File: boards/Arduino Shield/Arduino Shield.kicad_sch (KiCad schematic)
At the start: 22 parts, among them J1 Screw_Terminal_01x07, J10 Screw_Terminal_01x03, J11 Screw_Terminal_01x08, J2 Screw_Terminal_01x08, J3 Screw_Terminal_01x08, J4 Screw_Terminal_01x08, J5 Screw_Terminal_01x08, J6 Screw_Terminal_01x08, J7 Screw_Terminal_01x08, J8 Screw_Terminal_01x04, J9 Screw_Terminal_01x10, U1 A000062

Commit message: Fixed pcb and schematic.
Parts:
- removed J10: Screw_Terminal_01x03, TerminalBlock_4Ucon:TerminalBlock_4Ucon_1x03_P3.50mm_Horizontal, symbol Connector:Screw_Terminal_01x03
- removed J8: Screw_Terminal_01x04, TerminalBlock_4Ucon:TerminalBlock_4Ucon_1x04_P3.50mm_Horizontal, symbol Connector:Screw_Terminal_01x04
- added J8: Screw_Terminal_01x07, TerminalBlock_4Ucon:TerminalBlock_4Ucon_1x07_P3.50mm_Horizontal, symbol Connector:Screw_Terminal_01x07
- R4: value 230Ω -> 232Ω
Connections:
- net at U1.43 (D43): now also J8.4 (Pin_4)
- net at U1.45 (D45): now also J8.5 (Pin_5)
- net at U1.47 (D47): now also J8.6 (Pin_6)
- net at U1.GND5: now also J8.7 (Pin_7)
- net at U1.37 (D37): now also J8.1 (Pin_1)
- net at U1.39 (D39): now also J8.2 (Pin_2)
- net at U1.41 (D41): now also J8.3 (Pin_3)

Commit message: finished shield v1
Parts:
- renumbered D3 to D1, D4 to D2, D2 to D3, D5 to D4, D1 to D5
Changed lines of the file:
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@@
   (symbol (lib_id "Device:LED") (at 87.63 154.94 90) (unit 1)
     (in_bom yes) (on_board yes) (dnp no)
-    (property "Reference" "D5" (at 91.44 156.21 90)
+    (property "Reference" "D4" (at 91.44 156.21 90)
       (effects (font (size 1.27 1.27)))
     )
@@
       (project "Arduino Shield"
         (path "/d32bdb2e-fa3a-461a-9e34-c0053c91b5d5"
-          (reference "D5") (unit 1)
+          (reference "D4") (unit 1)
         )
       )
@@
   (symbol (lib_id "Device:LED") (at 162.56 153.67 90) (unit 1)
     (in_bom yes) (on_board yes) (dnp no) (fields_autoplaced)
-    (property "Reference" "D2" (at 166.37 153.9875 90)
+    (property "Reference" "D3" (at 166.37 153.9875 90)
       (effects (font (size 1.27 1.27)) (justify right))
     )
@@
       (project "Arduino Shield"
         (path "/d32bdb2e-fa3a-461a-9e34-c0053c91b5d5"
-          (reference "D2") (unit 1)
+          (reference "D3") (unit 1)
         )
       )
@@
   (symbol (lib_id "Device:LED") (at 154.94 158.75 90) (unit 1)
     (in_bom yes) (on_board yes) (dnp no) (fields_autoplaced)
-    (property "Reference" "D1" (at 158.75 159.0675 90)
+    (property "Reference" "D5" (at 158.75 159.0675 90)
       (effects (font (size 1.27 1.27)) (justify right))
     )
@@
       (project "Arduino Shield"
         (path "/d32bdb2e-fa3a-461a-9e34-c0053c91b5d5"
+          (reference "D5") (unit 1)
+        )
+      )
+    )
+  )
+  (symbol (lib_id "Device:LED") (at 170.18 149.86 90) (unit 1)
+    (in_bom yes) (on_board yes) (dnp no) (fields_autoplaced)
+    (property "Reference" "D1" (at 173.99 150.1775 90)
+      (effects (font (size 1.27 1.27)) (justify right))
+    )
+    (property "Value" "LED" (at 173.99 152.7175 90)
+      (effects (font (size 1.27 1.27)) (justify right))
+    )
+    (property "Footprint" "LED_SMD:LED_0805_2012Metric" (at 170.18 149.86 0)
+      (effects (font (size 1.27 1.27)) hide)
+    )
+    (property "Datasheet" "https://www.mouser.com/datasheet/2/216/APT2012QBC_D-226241.pdf" (at 170.18 149.86 0)
+      (effects (font (size 1.27 1.27)) hide)
+    )
+    (pin "1")
+    (pin "2")
+    (instances
+      (project "Arduino Shield"
+        (path "/d32bdb2e-fa3a-461a-9e34-c0053c91b5d5"
           (reference "D1") (unit 1)
-        )
-      )
-    )
-  )
-  (symbol (lib_id "Device:LED") (at 170.18 149.86 90) (unit 1)
-    (in_bom yes) (on_board yes) (dnp no) (fields_autoplaced)
-    (property "Reference" "D3" (at 173.99 150.1775 90)
-      (effects (font (size 1.27 1.27)) (justify right))
-    )
-    (property "Value" "LED" (at 173.99 152.7175 90)
-      (effects (font (size 1.27 1.27)) (justify right))
-    )
-    (property "Footprint" "LED_SMD:LED_0805_2012Metric" (at 170.18 149.86 0)
-      (effects (font (size 1.27 1.27)) hide)
-    )
-    (property "Datasheet" "https://www.mouser.com/datasheet/2/216/APT2012QBC_D-226241.pdf" (at 170.18 149.86 0)
-      (effects (font (size 1.27 1.27)) hide)
-    )
-    (pin "1")
-    (pin "2")
-    (instances
-      (project "Arduino Shield"
-        (path "/d32bdb2e-fa3a-461a-9e34-c0053c91b5d5"
-          (reference "D3") (unit 1)
         )
       )
@@
   (symbol (lib_id "Device:LED") (at 85.09 157.48 90) (unit 1)
     (in_bom yes) (on_board yes) (dnp no)
-    (property "Reference" "D4" (at 81.28 158.75 90)
+    (property "Reference" "D2" (at 81.28 158.75 90)
       (effects (font (size 1.27 1.27)))
     )
@@
       (project "Arduino Shield"
         (path "/d32bdb2e-fa3a-461a-9e34-c0053c91b5d5"
-          (reference "D4") (unit 1)
-        )
-      )
+          (reference "D2") (unit 1)
+        )
+      )

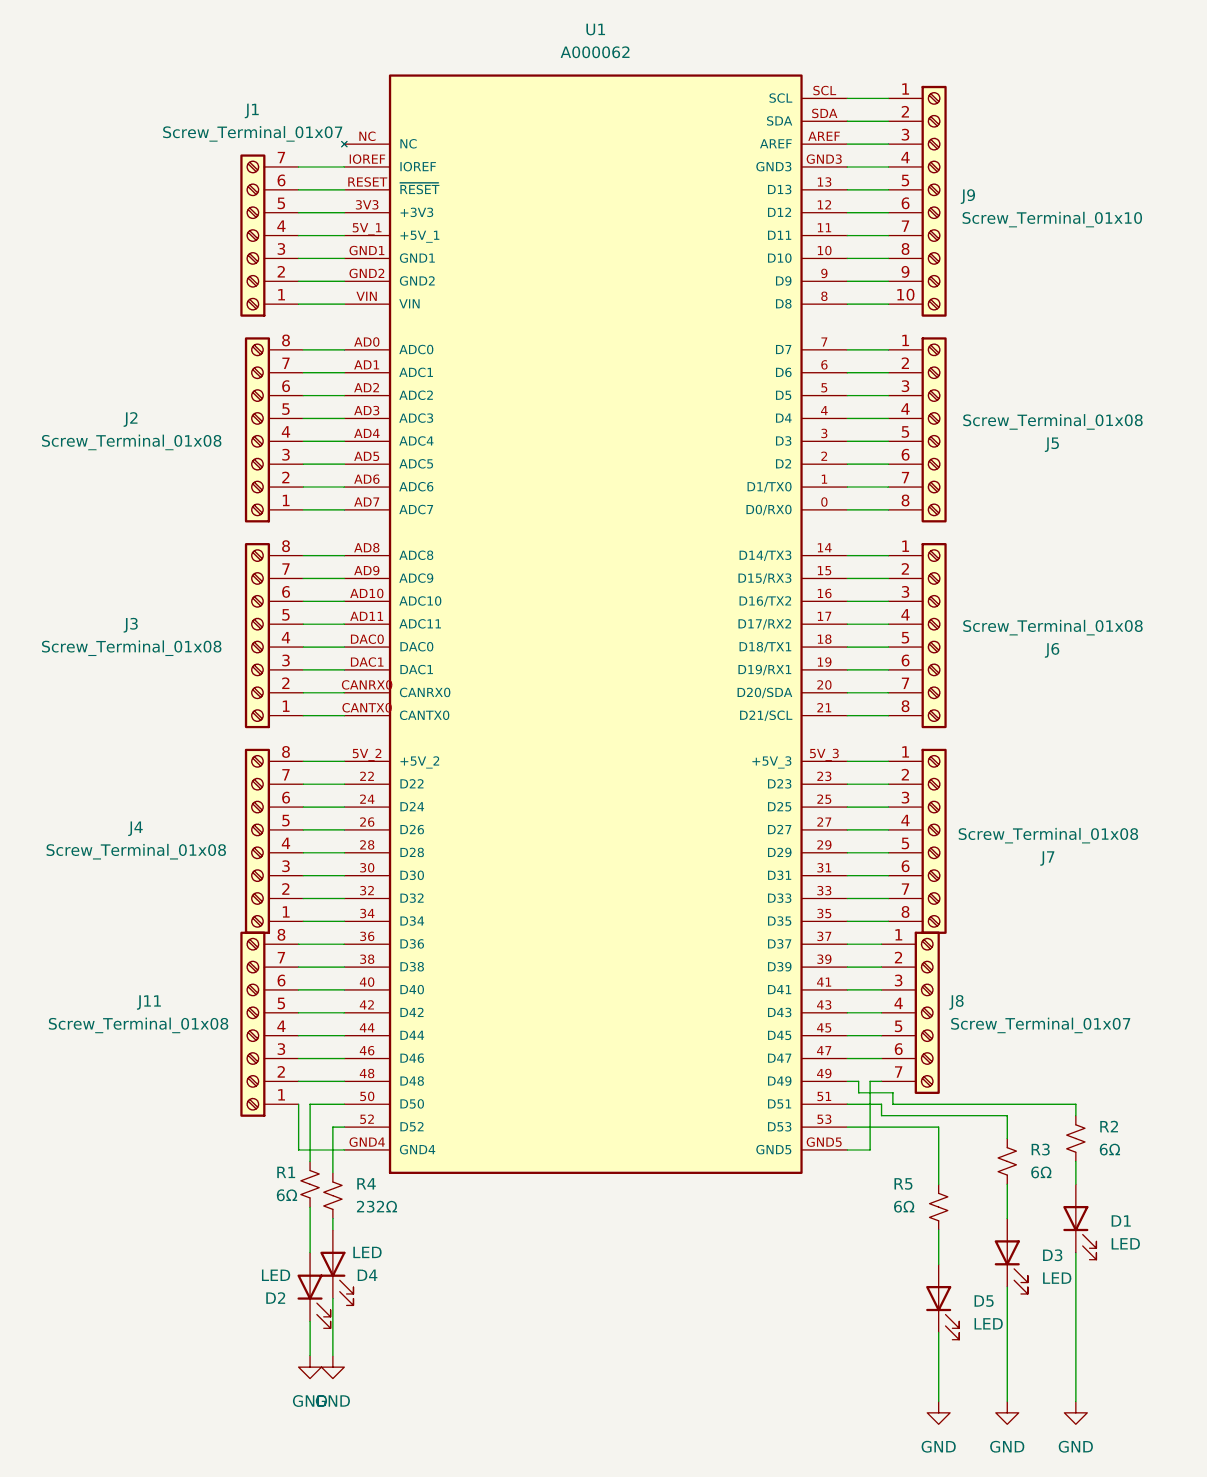
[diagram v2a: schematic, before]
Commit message: Add GND
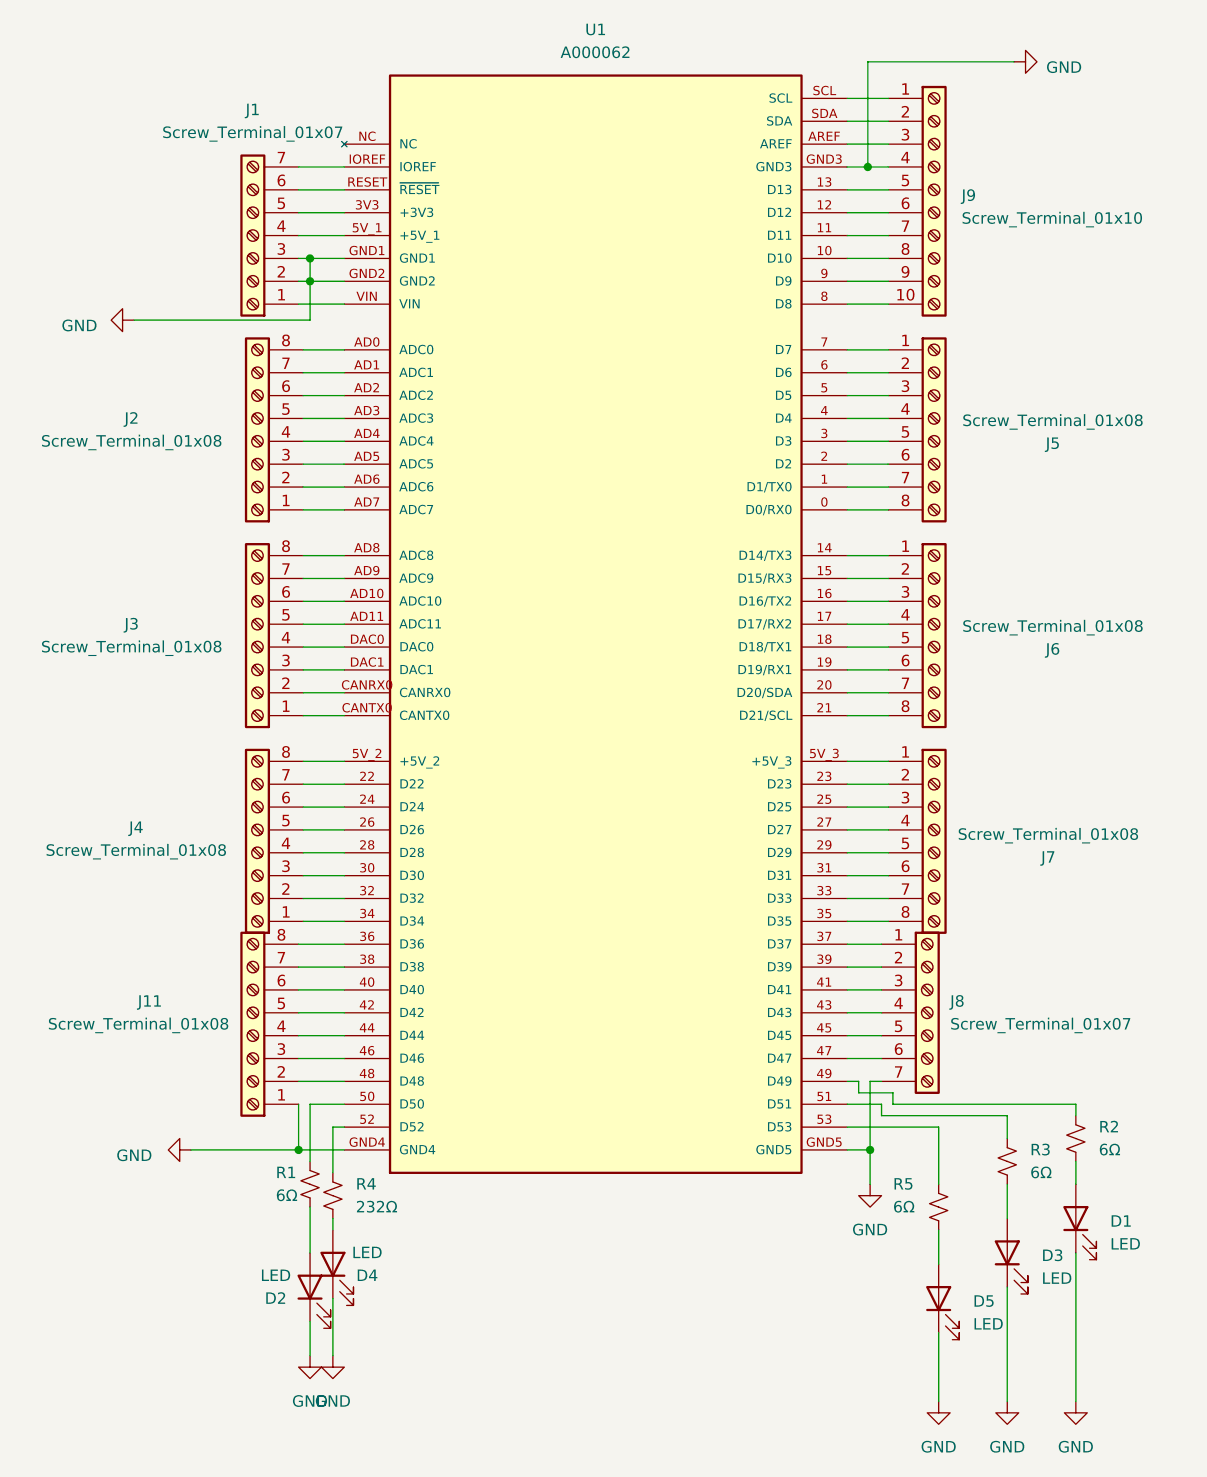
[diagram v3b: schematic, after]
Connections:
- net GND: now also J1.2 (Pin_2), J1.3 (Pin_3), J11.1 (Pin_1), J8.7 (Pin_7), J9.4 (Pin_4), U1.GND1, U1.GND2, U1.GND3, U1.GND4, U1.GND5
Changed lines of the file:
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@@
 (kicad_sch (version 20230121) (generator eeschema)
   (paper "A4")
+  (junction (at 147.32 142.24) (diameter 0) (color 0 0 0 0)
+  )
+  (junction (at 147.066 33.02) (diameter 0) (color 0 0 0 0)
+  )
+  (junction (at 85.09 45.72) (diameter 0) (color 0 0 0 0)
+  )
+  (junction (at 83.82 142.24) (diameter 0) (color 0 0 0 0)
+  )
+  (junction (at 85.09 43.18) (diameter 0) (color 0 0 0 0)
+  )
   (wire (pts (xy 149.352 101.6) (xy 144.78 101.6))
     (stroke (width 0) (type default))
@@
     (stroke (width 0) (type default))
   )
+  (wire (pts (xy 147.066 33.02) (xy 149.352 33.02))
+    (stroke (width 0) (type default))
+  )
   (wire (pts (xy 88.9 124.46) (xy 83.82 124.46))
     (stroke (width 0) (type default))
@@
     (stroke (width 0) (type default))
   )
+  (wire (pts (xy 65.532 50.038) (xy 85.09 50.038))
+    (stroke (width 0) (type default))
+  )
   (wire (pts (xy 148.59 137.16) (xy 148.59 138.43))
     (stroke (width 0) (type default))
@@
     (stroke (width 0) (type default))
   )
-  (wire (pts (xy 83.82 142.24) (xy 83.82 137.16))
+  (wire (pts (xy 83.82 137.16) (xy 83.82 142.24))
+    (stroke (width 0) (type default))
+  )
+  (wire (pts (xy 85.09 50.038) (xy 85.09 45.72))
     (stroke (width 0) (type default))
   )
@@
     (stroke (width 0) (type default))
   )
+  (wire (pts (xy 147.32 142.24) (xy 147.32 146.05))
+    (stroke (width 0) (type default))
+  )
   (wire (pts (xy 149.352 68.58) (xy 144.78 68.58))
     (stroke (width 0) (type default))
   )
+  (wire (pts (xy 163.322 21.336) (xy 147.066 21.336))
+    (stroke (width 0) (type default))
+  )
   (wire (pts (xy 84.328 99.06) (xy 88.9 99.06))
     (stroke (width 0) (type default))
@@
     (stroke (width 0) (type default))
   )
-  (wire (pts (xy 83.82 43.18) (xy 88.9 43.18))
+  (wire (pts (xy 83.82 43.18) (xy 85.09 43.18))
     (stroke (width 0) (type default))
   )
@@
     (stroke (width 0) (type default))
   )
-  (wire (pts (xy 144.78 33.02) (xy 149.352 33.02))
+  (wire (pts (xy 144.78 33.02) (xy 147.066 33.02))
+    (stroke (width 0) (type default))
+  )
+  (wire (pts (xy 85.09 43.18) (xy 85.09 45.72))
     (stroke (width 0) (type default))
   )
@@
     (stroke (width 0) (type default))
   )
+  (wire (pts (xy 71.882 142.24) (xy 83.82 142.24))
+    (stroke (width 0) (type default))
+  )
   (wire (pts (xy 84.328 71.12) (xy 88.9 71.12))
     (stroke (width 0) (type default))
@@
     (stroke (width 0) (type default))
   )
+  (wire (pts (xy 85.09 45.72) (xy 88.9 45.72))
+    (stroke (width 0) (type default))
+  )
   (wire (pts (xy 83.82 48.26) (xy 88.9 48.26))
     (stroke (width 0) (type default))
@@
     (stroke (width 0) (type default))
   )
+  (wire (pts (xy 85.09 43.18) (xy 88.9 43.18))
+    (stroke (width 0) (type default))
+  )
   (wire (pts (xy 162.56 146.05) (xy 162.56 149.86))
     (stroke (width 0) (type default))
@@
     (stroke (width 0) (type default))
   )
-  (wire (pts (xy 83.82 45.72) (xy 88.9 45.72))
+  (wire (pts (xy 83.82 45.72) (xy 85.09 45.72))
     (stroke (width 0) (type default))
   )
@@
   )
   (wire (pts (xy 149.352 58.42) (xy 144.78 58.42))
+    (stroke (width 0) (type default))
+  )
+  (wire (pts (xy 147.066 21.336) (xy 147.066 33.02))
     (stroke (width 0) (type default))
   )
@@
     )
   )
+  (symbol (lib_id "power:GND") (at 163.322 21.336 90) (unit 1)
+    (in_bom yes) (on_board yes) (dnp no) (fields_autoplaced)
+    (property "Reference" "#PWR09" (at 169.672 21.336 0)
+      (effects (font (size 1.27 1.27)) hide)
+    )
+    (property "Value" "GND" (at 166.878 21.971 90)
+      (effects (font (size 1.27 1.27)) (justify right))
+    )
+    (property "Footprint" "" (at 163.322 21.336 0)
+      (effects (font (size 1.27 1.27)) hide)
+    )
+    (property "Datasheet" "" (at 163.322 21.336 0)
+      (effects (font (size 1.27 1.27)) hide)
+    )
+    (pin "1")
+    (instances
+      (project "Arduino Shield"
+        (path "/d32bdb2e-fa3a-461a-9e34-c0053c91b5d5"
+          (reference "#PWR09") (unit 1)
+        )
+      )
+    )
+  )
   (symbol (lib_id "Connector:Screw_Terminal_01x07") (at 78.74 40.64 180) (unit 1)
     (in_bom yes) (on_board yes) (dnp no) (fields_autoplaced)
@@
     )
   )
+  (symbol (lib_id "power:GND") (at 65.532 50.038 270) (unit 1)
+    (in_bom yes) (on_board yes) (dnp no) (fields_autoplaced)
+    (property "Reference" "#PWR06" (at 59.182 50.038 0)
+      (effects (font (size 1.27 1.27)) hide)
+    )
+    (property "Value" "GND" (at 61.468 50.673 90)
+      (effects (font (size 1.27 1.27)) (justify right))
+    )
+    (property "Footprint" "" (at 65.532 50.038 0)
+      (effects (font (size 1.27 1.27)) hide)
+    )
+    (property "Datasheet" "" (at 65.532 50.038 0)
+      (effects (font (size 1.27 1.27)) hide)
+    )
+    (pin "1")
+    (instances
+      (project "Arduino Shield"
+        (path "/d32bdb2e-fa3a-461a-9e34-c0053c91b5d5"
+          (reference "#PWR06") (unit 1)
+        )
+      )
+    )
+  )
   (symbol (lib_id "power:GND") (at 85.09 165.1 0) (unit 1)
     (in_bom yes) (on_board yes) (dnp no) (fields_autoplaced)
@@
     )
   )
+  (symbol (lib_id "power:GND") (at 147.32 146.05 0) (unit 1)
+    (in_bom yes) (on_board yes) (dnp no) (fields_autoplaced)
+    (property "Reference" "#PWR08" (at 147.32 152.4 0)
+      (effects (font (size 1.27 1.27)) hide)
+    )
+    (property "Value" "GND" (at 147.32 151.13 0)
+      (effects (font (size 1.27 1.27)))
+    )
+    (property "Footprint" "" (at 147.32 146.05 0)
+      (effects (font (size 1.27 1.27)) hide)
+    )
+    (property "Datasheet" "" (at 147.32 146.05 0)
+      (effects (font (size 1.27 1.27)) hide)
+    )
+    (pin "1")
+    (instances
+      (project "Arduino Shield"
+        (path "/d32bdb2e-fa3a-461a-9e34-c0053c91b5d5"
+          (reference "#PWR08") (unit 1)
+        )
+      )
+    )
+  )
   (symbol (lib_id "Device:LED") (at 162.56 153.67 90) (unit 1)
     (in_bom yes) (on_board yes) (dnp no) (fields_autoplaced)
@@
         )
       )
+    )
+  )
+  (symbol (lib_id "power:GND") (at 71.882 142.24 270) (unit 1)
+    (in_bom yes) (on_board yes) (dnp no) (fields_autoplaced)
+    (property "Reference" "#PWR07" (at 65.532 142.24 0)
+      (effects (font (size 1.27 1.27)) hide)
+    )
+    (property "Value" "GND" (at 67.564 142.875 90)
+      (effects (font (size 1.27 1.27)) (justify right))
+    )
+    (property "Footprint" "" (at 71.882 142.24 0)
+      (effects (font (size 1.27 1.27)) hide)
+    )
+    (property "Datasheet" "" (at 71.882 142.24 0)
+      (effects (font (size 1.27 1.27)) hide)
+    )
+    (pin "1")
+    (instances
+      (project "Arduino Shield"
+        (path "/d32bdb2e-fa3a-461a-9e34-c0053c91b5d5"
+          (reference "#PWR07") (unit 1)
+        )
+      )
